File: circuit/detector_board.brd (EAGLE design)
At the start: 60 x 60 mm, 10 parts

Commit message: boards: Rev00_ds ready
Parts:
- moved C4 26.6 mm to (32.6, 30.1), flipped to the bottom, turned to 0 degrees
- moved C3 23.2 mm to (32.6, 27.2), flipped to the bottom, turned to 0 degrees
- moved C2 20.0 mm to (32.6, 24.3), flipped to the bottom, turned to 0 degrees
- moved R2 15.9 mm to (32.6, 20.2), flipped to the bottom, turned to 0 degrees
- moved C1 13.9 mm to (32.6, 17.6), flipped to the bottom, turned to 0 degrees
- moved R1 12.7 mm to (32.6, 15.0), flipped to the bottom, turned to 180 degrees
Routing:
- net VBIAS: track 41.1 -> 18.4 mm, vias 0 -> 1
- net N$4: track 3.56 -> 17.7 mm
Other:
- board text added: "Rev00_ds, detector board Asher Merrill & Maurik Holtrop, UNH 2018"
- board text removed: "Rev00_ss, detector board Asher Merrill & Maurik Holtrop, UNH 2018"
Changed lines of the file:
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@@
 <drawing>
 <settings>
-<setting alwaysvectorfont="no"/>
+<setting alwaysvectorfont="yes"/>
 <setting verticaltext="up"/>
 </settings>
@@
 <text x="44.5" y="2.5" size="1.778" layer="21">Vbias</text>
 <text x="44.5" y="4.5" size="1.778" layer="21">Gnd</text>
-<text x="43" y="58" size="1.2" layer="21" rot="R180">Rev00_ss, detector board
+<text x="43" y="58" size="1.2" layer="21" rot="R180">Rev00_ds, detector board
 Asher Merrill &amp; Maurik Holtrop, UNH 2018</text>
 </plain>
@@
 </autorouter>
 <elements>
-<element name="R1" library="rcl" library_urn="urn:adsk.eagle:library:334" package="R0805" package3d_urn="urn:adsk.eagle:package:23553/2" value="49.9" x="39.49" y="4.4" smashed="yes" rot="R90">
-<attribute name="NAME" x="39.97" y="6.615" size="1.27" layer="25" rot="R90"/>
-<attribute name="SPICEPREFIX" value="R" x="39.49" y="4.4" size="1.778" layer="27" rot="R90" display="off"/>
-</element>
-<element name="R2" library="rcl" library_urn="urn:adsk.eagle:library:334" package="R0805" package3d_urn="urn:adsk.eagle:package:23553/2" value="49.9" x="34.29" y="4.4" smashed="yes" rot="R270">
-<attribute name="NAME" x="34.75" y="6.615" size="1.27" layer="25" rot="R90"/>
-<attribute name="SPICEPREFIX" value="R" x="34.29" y="4.4" size="1.778" layer="27" rot="R270" display="off"/>
+<element name="R1" library="rcl" library_urn="urn:adsk.eagle:library:334" package="R0805" package3d_urn="urn:adsk.eagle:package:23553/2" value="49.9" x="32.6" y="15.01" smashed="yes" rot="MR180">
+<attribute name="NAME" x="34.815" y="15.49" size="1.27" layer="26" rot="MR180"/>
+<attribute name="SPICEPREFIX" value="R" x="32.6" y="15.01" size="1.778" layer="28" rot="MR180" display="off"/>
+</element>
+<element name="R2" library="rcl" library_urn="urn:adsk.eagle:library:334" package="R0805" package3d_urn="urn:adsk.eagle:package:23553/2" value="49.9" x="32.6" y="20.21" smashed="yes" rot="MR0">
+<attribute name="NAME" x="34.815" y="20.67" size="1.27" layer="26" rot="MR180"/>
+<attribute name="SPICEPREFIX" value="R" x="32.6" y="20.21" size="1.778" layer="28" rot="MR0" display="off"/>
 </element>
 <element name="R3" library="rcl" library_urn="urn:adsk.eagle:library:334" package="R0805" package3d_urn="urn:adsk.eagle:package:23553/2" value="49.9" x="19.59" y="6.41" smashed="yes" rot="R180">
@@
 <attribute name="SPICEPREFIX" value="R" x="19.59" y="6.41" size="1.778" layer="27" rot="R180" display="off"/>
 </element>
-<element name="C1" library="rcl" package="C0805" value="10nF" x="36.89" y="4.4" smashed="yes" rot="R270">
-<attribute name="NAME" x="37.4" y="6.58" size="1.27" layer="25" rot="R90"/>
-</element>
-<element name="C2" library="rcl" package="C0805" value="10nF" x="30.79" y="4.4" smashed="yes" rot="R270">
-<attribute name="NAME" x="31.3" y="6.58" size="1.27" layer="25" rot="R90"/>
-</element>
-<element name="C3" library="rcl" package="C0805" value="10nF" x="28.19" y="4.4" smashed="yes" rot="R270">
-<attribute name="NAME" x="28.7" y="6.58" size="1.27" layer="25" rot="R90"/>
-</element>
-<element name="C4" library="rcl" package="C0805" value="10nF" x="25.59" y="4.4" smashed="yes" rot="R270">
-<attribute name="NAME" x="26.09" y="6.63" size="1.27" layer="25" rot="R90"/>
+<element name="C1" library="rcl" package="C0805" value="10nF" x="32.6" y="17.61" smashed="yes" rot="MR0">
+<attribute name="NAME" x="34.78" y="18.12" size="1.27" layer="26" rot="MR180"/>
+</element>
+<element name="C2" library="rcl" package="C0805" value="10nF" x="32.6" y="24.29" smashed="yes" rot="MR0">
+<attribute name="NAME" x="34.78" y="24.8" size="1.27" layer="26" rot="MR180"/>
+</element>
+<element name="C3" library="rcl" package="C0805" value="10nF" x="32.6" y="27.19" smashed="yes" rot="MR0">
+<attribute name="NAME" x="34.78" y="27.7" size="1.27" layer="26" rot="MR180"/>
+</element>
+<element name="C4" library="rcl" package="C0805" value="10nF" x="32.6" y="30.09" smashed="yes" rot="MR0">
+<attribute name="NAME" x="34.83" y="30.59" size="1.27" layer="26" rot="MR180"/>
 </element>
 <element name="J$1" library="SparkFun-Retired" package="SMA-EDGE" value="SMA_EDGE" x="15" y="2.5"/>
@@
 <contactref element="R2" pad="1"/>
 <contactref element="C1" pad="1"/>
-<wire x1="39.49" y1="5.35" x2="36.89" y2="5.35" width="0.3048" layer="1"/>
-<wire x1="36.89" y1="5.35" x2="34.29" y2="5.35" width="0.3048" layer="1"/>
+<wire x1="33.55" y1="17.61" x2="33.55" y2="20.21" width="0.3048" layer="16"/>
+<wire x1="33.55" y1="17.61" x2="33.55" y2="15.01" width="0.3048" layer="16"/>
 </signal>
 <signal name="VBIAS">
@@
 <contactref element="C3" pad="1"/>
 <contactref element="C2" pad="1"/>
-<wire x1="34.29" y1="3.45" x2="34.1" y2="3.45" width="0.3048" layer="1"/>
-<wire x1="34.29" y1="3.45" x2="33.55" y2="3.45" width="0.3048" layer="1"/>
-<wire x1="31.65" y1="5.35" x2="30.79" y2="5.35" width="0.3048" layer="1"/>
-<wire x1="33.55" y1="3.45" x2="31.65" y2="5.35" width="0.3048" layer="1"/>
-<wire x1="30.79" y1="5.35" x2="28.19" y2="5.35" width="0.3048" layer="1"/>
-<wire x1="28.19" y1="5.35" x2="25.59" y2="5.35" width="0.3048" layer="1"/>
-<wire x1="30.79" y1="5.35" x2="30.79" y2="17.79" width="0.3048" layer="1"/>
-<wire x1="30.79" y1="17.79" x2="35.5" y2="22.5" width="0.3048" layer="1"/>
-<wire x1="35.5" y1="22.5" x2="35.5" y2="31.752" width="0.3048" layer="1"/>
-<wire x1="34.327" y1="32.925" x2="35.5" y2="31.752" width="0.305" layer="1"/>
 <contactref element="FC-600XX-1" pad="N_CATH"/>
-<wire x1="32.925" y1="32.925" x2="34.327" y2="32.925" width="0.3048" layer="1"/>
+<wire x1="31.65" y1="20.21" x2="31.65" y2="20.65" width="0.3048" layer="16"/>
+<wire x1="33.55" y1="22.55" x2="33.55" y2="24.29" width="0.3048" layer="16"/>
+<wire x1="31.65" y1="20.65" x2="33.55" y2="22.55" width="0.3048" layer="16"/>
+<wire x1="33.55" y1="24.29" x2="33.55" y2="27.19" width="0.3048" layer="16"/>
+<wire x1="33.55" y1="27.19" x2="33.55" y2="30.09" width="0.3048" layer="16"/>
+<via x="36.5" y="31.5" extent="1-16" drill="0.35"/>
+<wire x1="33.55" y1="30.09" x2="35.09" y2="30.09" width="0.3048" layer="16"/>
+<wire x1="35.09" y1="30.09" x2="36.5" y2="31.5" width="0.3048" layer="16"/>
+<wire x1="32.925" y1="32.925" x2="35.075" y2="32.925" width="0.3048" layer="1"/>
+<wire x1="35.075" y1="32.925" x2="36.5" y2="31.5" width="0.3048" layer="1"/>
 </signal>
 <signal name="GND">
@@
 <contactref element="SRC" pad="1"/>
 <contactref element="R1" pad="1"/>
-<wire x1="39.49" y1="3.45" x2="43.05" y2="3.45" width="0.3048" layer="1"/>
+<wire x1="31.65" y1="15.01" x2="31.65" y2="12.35" width="0.3048" layer="16"/>
+<wire x1="40.55" y1="3.45" x2="43.05" y2="3.45" width="0.3048" layer="16"/>
+<wire x1="31.65" y1="12.35" x2="40.55" y2="3.45" width="0.3048" layer="16"/>
 </signal>
 </signals>

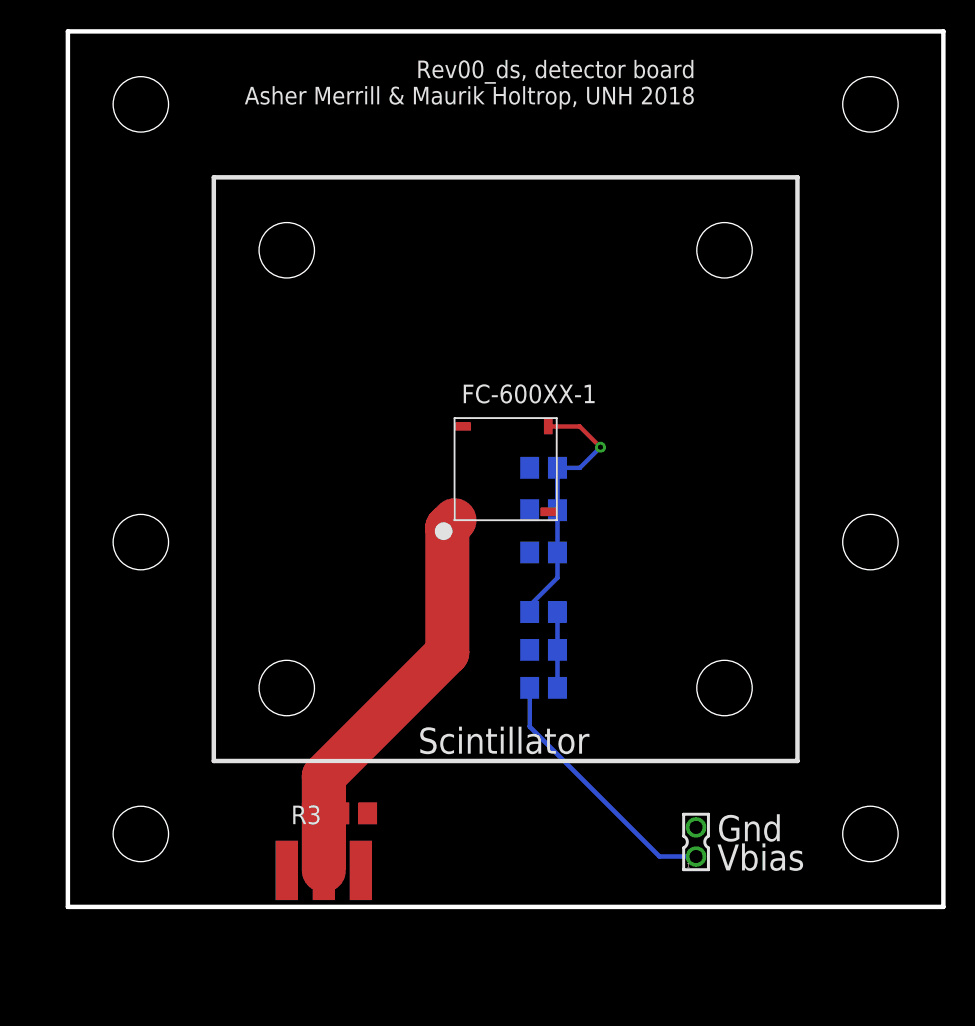
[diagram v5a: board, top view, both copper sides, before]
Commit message: boards: Changed packages of cap and resistors to be 0603, as we will have available.  Also changed mount points to be grounded, and made vias solderable.
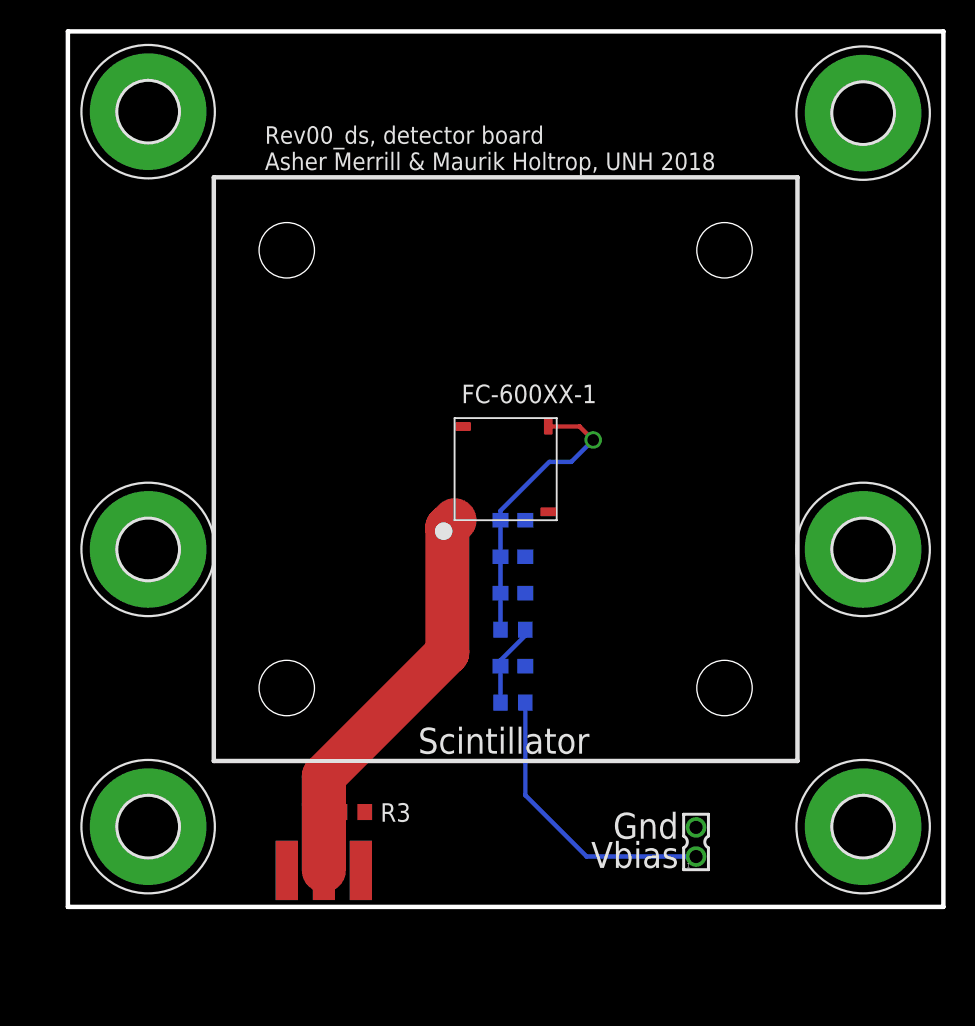
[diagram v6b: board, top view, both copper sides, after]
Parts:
- added H1, H2, H3, H4, H5, H6: MOUNT-PAD-ROUND4.1, holes:4,1-PAD
- C1, C2, C3, C4: device rcl:C0805 -> rcl:C0603
- R1, R2, R3: device rcl:R0805 -> rcl:R0603
- moved C4 6.44 mm to (30.5, 24.0), turned to 180 degrees
- moved C2 3.49 mm to (30.5, 21.5), turned to 180 degrees
- moved R2 2.42 mm to (30.5, 19.0)
- moved C1 2.38 mm to (30.5, 16.5), turned to 180 degrees
- moved R1 2.33 mm to (30.5, 14.0), turned to 0 degrees
- moved C3 2.21 mm to (30.5, 26.5), turned to 180 degrees
- moved R3 0.13 mm to (19.5, 6.50)
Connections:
- net GND: now also H1.B4,1, H2.B4,1, H3.B4,1, H4.B4,1, H5.B4,1, H6.B4,1
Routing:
- net N$4: track 17.7 -> 19.8 mm
- net VBIAS: track 18.4 -> 20.0 mm
- net N$1: track 5.20 -> 5.70 mm
